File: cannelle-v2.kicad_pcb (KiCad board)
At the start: 2 copper layers, 62 parts, among them P1 USB_OTG, P2 CONN_02X04, P3 CONN_02X22, P4 CONN_02X22, SW1 SW_PUSH, U1 74LS157, U2 ATMEGA16U4-A, U3 SST25VF020B, U4 LD1117S12TR, U5 NCP1117ST33T3G, U6 ICE40HX1K-VQ100, X1 8MHz, X2 IQXO/7X

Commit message: Place components on PCB
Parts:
- moved C14 101.3 mm to (155.8, 40.9)
- moved C21 95.7 mm to (138.8, 52.1), turned to 180 degrees
- moved C20 94.4 mm to (139.8, 50.7), turned to 180 degrees
- moved C30 89.1 mm to (154.2, 53.7)
- moved C23 87.4 mm to (152.4, 51.8), turned to 90 degrees
- moved C24 86.0 mm to (155.4, 55.1)
- moved R11 85.9 mm to (132.5, 51.1), turned to 180 degrees
- moved R10 84.6 mm to (125.5, 63.9), turned to 90 degrees
- moved R12 80.6 mm to (132.5, 53.1), turned to 180 degrees
- moved D3 75.9 mm to (125.5, 60.6), turned to 90 degrees
- moved R9 75.5 mm to (128.7, 63.9), turned to 90 degrees
- moved C18 74.8 mm to (140.0, 68.6), turned to 270 degrees
- moved C17 74.4 mm to (138.4, 67.1), turned to 270 degrees
- moved C22 74.2 mm to (141.2, 49.1), turned to 180 degrees
- moved C25 72.9 mm to (149.4, 49.1), turned to 90 degrees
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
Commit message: Correct wrong label on schem and PCB
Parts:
- moved R7 5.41 mm to (160.1, 79.2), turned to 270 degrees
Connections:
- U1 pad 13: /FPAG_SS -> /FPGA_SS
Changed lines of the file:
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@@
 (kicad_pcb (version 4) (host pcbnew 4.0.2-stable)
   (general
-    (links 254)
-    (no_connects 254)
-    (area 108.667476 35.225999 198.545524 144.534)
+    (links 255)
+    (no_connects 255)
+    (area 0 0 0 0)
     (thickness 1.6)
     (drawings 0)
@@
     (zones 0)
     (modules 62)
-    (nets 134)
+    (nets 133)
   )
   (page A4)
@@
   (net 115 "Net-(U1-Pad11)")
   (net 116 /FLASH_SS)
-  (net 117 /FPAG_SS)
-  (net 118 "Net-(U2-Pad1)")
-  (net 119 "Net-(U2-Pad2)")
-  (net 120 "Net-(U2-Pad12)")
-  (net 121 "Net-(U2-Pad15)")
-  (net 122 "Net-(U2-Pad18)")
-  (net 123 "Net-(U2-Pad19)")
-  (net 124 "Net-(U2-Pad22)")
-  (net 125 "Net-(U2-Pad23)")
-  (net 126 "Net-(U2-Pad25)")
-  (net 127 "Net-(U2-Pad31)")
-  (net 128 "Net-(U2-Pad32)")
-  (net 129 "Net-(U2-Pad33)")
-  (net 130 "Net-(U2-Pad35)")
-  (net 131 /CS_FLASH)
-  (net 132 /FPGA/SYS_CLK)
-  (net 133 "Net-(U6-Pad76)")
+  (net 117 "Net-(U2-Pad1)")
+  (net 118 "Net-(U2-Pad2)")
+  (net 119 "Net-(U2-Pad12)")
+  (net 120 "Net-(U2-Pad15)")
+  (net 121 "Net-(U2-Pad18)")
+  (net 122 "Net-(U2-Pad19)")
+  (net 123 "Net-(U2-Pad22)")
+  (net 124 "Net-(U2-Pad23)")
+  (net 125 "Net-(U2-Pad25)")
+  (net 126 "Net-(U2-Pad31)")
+  (net 127 "Net-(U2-Pad32)")
+  (net 128 "Net-(U2-Pad33)")
+  (net 129 "Net-(U2-Pad35)")
+  (net 130 /CS_FLASH)
+  (net 131 /FPGA/SYS_CLK)
+  (net 132 "Net-(U6-Pad76)")
   (net_class Default "This is the default net class."
     (clearance 0.2)
@@
     (add_net /FLASH_SCK)
     (add_net /FLASH_SS)
-    (add_net /FPAG_SS)
     (add_net /FPGA/DONE)
     (add_net /FPGA/GPIO_3)
@@
   )
   (module Resistors_SMD:R_0402 (layer F.Cu)
-    (at 154.813 78.359)
+    (at 160.147 79.248 270)
     (descr "Resistor SMD 0402, reflow soldering, Vishay (see dcrcw.pdf)")
     (tags "resistor 0402")
     (attr smd)
-    (fp_text reference R7 (at 0 -1.8) (layer F.SilkS)
-      (effects (font (size 1 1) (thickness 0.15)))
-    )
-    (fp_text value 10k (at 0 1.8) (layer F.Fab)
+    (fp_text reference R7 (at 0 -1.8 270) (layer F.SilkS)
+      (effects (font (size 1 1) (thickness 0.15)))
+    )
+    (fp_text value 10k (at 0 1.8 270) (layer F.Fab)
       (effects (font (size 1 1) (thickness 0.15)))
     )
@@
     (fp_line (start 0.25 -0.525) (end -0.25 -0.525) (layer F.SilkS) (width 0.15))
     (fp_line (start -0.25 0.525) (end 0.25 0.525) (layer F.SilkS) (width 0.15))
-    (pad 1 smd rect (at -0.45 0) (size 0.4 0.6) (layers F.Cu F.Paste F.Mask)
-      (net 6 +3V3))
-    (pad 2 smd rect (at 0.45 0) (size 0.4 0.6) (layers F.Cu F.Paste F.Mask)
+    (pad 1 smd rect (at -0.45 0 270) (size 0.4 0.6) (layers F.Cu F.Paste F.Mask)
+      (net 6 +3V3))
+    (pad 2 smd rect (at 0.45 0 270) (size 0.4 0.6) (layers F.Cu F.Paste F.Mask)
       (net 84 /FPGA_SS))
     (model Resistors_SMD.3dshapes/R_0402.wrl
@@
       (net 116 /FLASH_SS))
     (pad 13 smd rect (at -0.635 -5.08) (size 0.635 1.905) (layers F.Cu F.Paste F.Mask)
-      (net 117 /FPAG_SS))
+      (net 84 /FPGA_SS))
     (pad 14 smd rect (at -1.905 -5.08) (size 0.635 1.905) (layers F.Cu F.Paste F.Mask)
       (net 110 /AVR_SS))
@@
     (fp_line (start -5.175 -4.5) (end -6.45 -4.5) (layer F.SilkS) (width 0.15))
     (pad 1 smd rect (at -5.7 -4) (size 1.5 0.55) (layers F.Cu F.Paste F.Mask)
-      (net 118 "Net-(U2-Pad1)"))
+      (net 117 "Net-(U2-Pad1)"))
     (pad 2 smd rect (at -5.7 -3.2) (size 1.5 0.55) (layers F.Cu F.Paste F.Mask)
-      (net 119 "Net-(U2-Pad2)"))
+      (net 118 "Net-(U2-Pad2)"))
     (pad 3 smd rect (at -5.7 -2.4) (size 1.5 0.55) (layers F.Cu F.Paste F.Mask)
       (net 108 "Net-(R3-Pad1)"))
@@
       (net 78 /MISO))
     (pad 12 smd rect (at -4 5.7 90) (size 1.5 0.55) (layers F.Cu F.Paste F.Mask)
-      (net 120 "Net-(U2-Pad12)"))
+      (net 119 "Net-(U2-Pad12)"))
     (pad 13 smd rect (at -3.2 5.7 90) (size 1.5 0.55) (layers F.Cu F.Paste F.Mask)
       (net 24 /RST_AVR))
@@
       (net 6 +3V3))
     (pad 15 smd rect (at -1.6 5.7 90) (size 1.5 0.55) (layers F.Cu F.Paste F.Mask)
-      (net 121 "Net-(U2-Pad15)"))
+      (net 120 "Net-(U2-Pad15)"))
     (pad 16 smd rect (at -0.8 5.7 90) (size 1.5 0.55) (layers F.Cu F.Paste F.Mask)
       (net 4 "Net-(C3-Pad1)"))
@@
       (net 3 "Net-(C2-Pad1)"))
     (pad 18 smd rect (at 0.8 5.7 90) (size 1.5 0.55) (layers F.Cu F.Paste F.Mask)
-      (net 122 "Net-(U2-Pad18)"))
+      (net 121 "Net-(U2-Pad18)"))
     (pad 19 smd rect (at 1.6 5.7 90) (size 1.5 0.55) (layers F.Cu F.Paste F.Mask)
-      (net 123 "Net-(U2-Pad19)"))
+      (net 122 "Net-(U2-Pad19)"))
     (pad 20 smd rect (at 2.4 5.7 90) (size 1.5 0.55) (layers F.Cu F.Paste F.Mask)
       (net 76 /AVR_RX))
@@
       (net 74 /AVR_TX))
     (pad 22 smd rect (at 4 5.7 90) (size 1.5 0.55) (layers F.Cu F.Paste F.Mask)
-      (net 124 "Net-(U2-Pad22)"))
+      (net 123 "Net-(U2-Pad22)"))
     (pad 23 smd rect (at 5.7 4) (size 1.5 0.55) (layers F.Cu F.Paste F.Mask)
-      (net 125 "Net-(U2-Pad23)"))
+      (net 124 "Net-(U2-Pad23)"))
     (pad 24 smd rect (at 5.7 3.2) (size 1.5 0.55) (layers F.Cu F.Paste F.Mask)
       (net 1 /AVCC))
     (pad 25 smd rect (at 5.7 2.4) (size 1.5 0.55) (layers F.Cu F.Paste F.Mask)
-      (net 126 "Net-(U2-Pad25)"))
+      (net 125 "Net-(U2-Pad25)"))
     (pad 26 smd rect (at 5.7 1.6) (size 1.5 0.55) (layers F.Cu F.Paste F.Mask)
       (net 103 /ADC6))
@@
       (net 25 /SPI_SELECT))
     (pad 31 smd rect (at 5.7 -2.4) (size 1.5 0.55) (layers F.Cu F.Paste F.Mask)
-      (net 127 "Net-(U2-Pad31)"))
+      (net 126 "Net-(U2-Pad31)"))
     (pad 32 smd rect (at 5.7 -3.2) (size 1.5 0.55) (layers F.Cu F.Paste F.Mask)
-      (net 128 "Net-(U2-Pad32)"))
+      (net 127 "Net-(U2-Pad32)"))
     (pad 33 smd rect (at 5.7 -4) (size 1.5 0.55) (layers F.Cu F.Paste F.Mask)
-      (net 129 "Net-(U2-Pad33)"))
+      (net 128 "Net-(U2-Pad33)"))
     (pad 34 smd rect (at 4 -5.7 90) (size 1.5 0.55) (layers F.Cu F.Paste F.Mask)
       (net 6 +3V3))
     (pad 35 smd rect (at 3.2 -5.7 90) (size 1.5 0.55) (layers F.Cu F.Paste F.Mask)
-      (net 130 "Net-(U2-Pad35)"))
+      (net 129 "Net-(U2-Pad35)"))
     (pad 36 smd rect (at 2.4 -5.7 90) (size 1.5 0.55) (layers F.Cu F.Paste F.Mask)
       (net 101 /ADC5))
@@
       (net 78 /MISO))
     (pad 1 smd rect (at -1.905 3.175) (size 0.508 1.143) (layers F.Cu F.Paste F.Mask)
-      (net 131 /CS_FLASH))
+      (net 130 /CS_FLASH))
     (model SMD_Packages.3dshapes/SOIC-8-N.wrl
       (at (xyz 0 0 0))
@@
       (net 6 +3V3))
     (pad 15 smd rect (at -7.7 1 225) (size 1.5 0.3) (layers F.Cu F.Paste F.Mask)
-      (net 132 /FPGA/SYS_CLK))
+      (net 131 /FPGA/SYS_CLK))
     (pad 16 smd rect (at -7.7 1.5 225) (size 1.5 0.3) (layers F.Cu F.Paste F.Mask)
       (net 94 "Net-(P4-Pad31)"))
@@
       (net 14 "Net-(D4-Pad1)"))
     (pad 76 smd rect (at 6 -7.7 315) (size 1.5 0.3) (layers F.Cu F.Paste F.Mask)
-      (net 133 "Net-(U6-Pad76)"))
+      (net 132 "Net-(U6-Pad76)"))
     (pad 77 smd rect (at 5.5 -7.7 315) (size 1.5 0.3) (layers F.Cu F.Paste F.Mask)
       (net 8 +1V2))
@@
       (net 2 GND))
     (pad 3 smd rect (at 2.49936 2.10058) (size 1.69926 2.14884) (layers F.Cu F.Paste F.Mask)
-      (net 132 /FPGA/SYS_CLK))
+      (net 131 /FPGA/SYS_CLK))
     (pad 4 smd rect (at 2.49936 -2.10058) (size 1.69926 2.14884) (layers F.Cu F.Paste F.Mask)
       (net 6 +3V3))

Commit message: Ordered labels
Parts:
- ?: renamed from P2; value CONN_02X04 -> (none)
- ?: renamed from P3; value CONN_02X22 -> (none)
- ?: renamed from P4; value CONN_02X22 -> (none)
- C1, C4, C5: value 1u -> (none)
- C10, C11, C12, C13, C14, C15, C16, C17, C18, C19, C20, C21, C22, C23, C24, C25, C26, C27, C28, C29, C30, C6, C7, C8, C9: value 100nF -> (none)
- C2, C3: value 22p -> (none)
- D1, D2, D3, D5: value LED -> (none)
- D4: value D_Schottky -> (none)
- R1: value 370 -> (none)
- R10, R12, R9: value 2.2k -> (none)
- R11, R4, R5, R7, R8: value 10k -> (none)
- R13, R2, R3: value 22 -> (none)
- R6: value 120 -> (none)
- SW1: value SW_PUSH -> (none)
- U1: value 74LS157 -> (none)
- U2: value ATMEGA16U4-A -> (none)
- U3: value SST25VF020B -> (none)
- U4: value LD1117S12TR -> (none)
- U5: value NCP1117ST33T3G -> (none)
- U6: value ICE40HX1K-VQ100 -> ICE40HX1K
- X1: value 8MHz -> (none)
- X2: value IQXO/7X -> (none)
- moved SW1 31.8 mm to (147.3, 101.1)
- moved C11 8.72 mm to (162.9, 84.5)
- moved C14 8.58 mm to (159.5, 48.6), turned to 45 degrees
- moved U3 8.54 mm to (161.4, 79.1)
- moved U1 8.03 mm to (159.6, 95.0)
- moved R5 7.80 mm to (156.2, 87.0)
- moved R8 7.80 mm to (157.7, 87.0)
- moved R7 7.78 mm to (159.4, 87.0)
- moved ? 7.56 mm to (169.2, 98.0)
- moved ? 6.56 mm to (118.0, 98.0)
- moved ? 5.79 mm to (150.1, 84.7)
- moved P1 3.94 mm to (132.2, 117.0)
- moved R2 3.01 mm to (131.4, 110.2)
- moved R3 3.01 mm to (133.0, 110.2)
- moved C17 2.87 mm to (136.4, 65.0), turned to 225 degrees
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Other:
- board text added: "Cannelle Project (c) Ronan Gailard 2016"
- board text added: "Made with love in Boston, US"

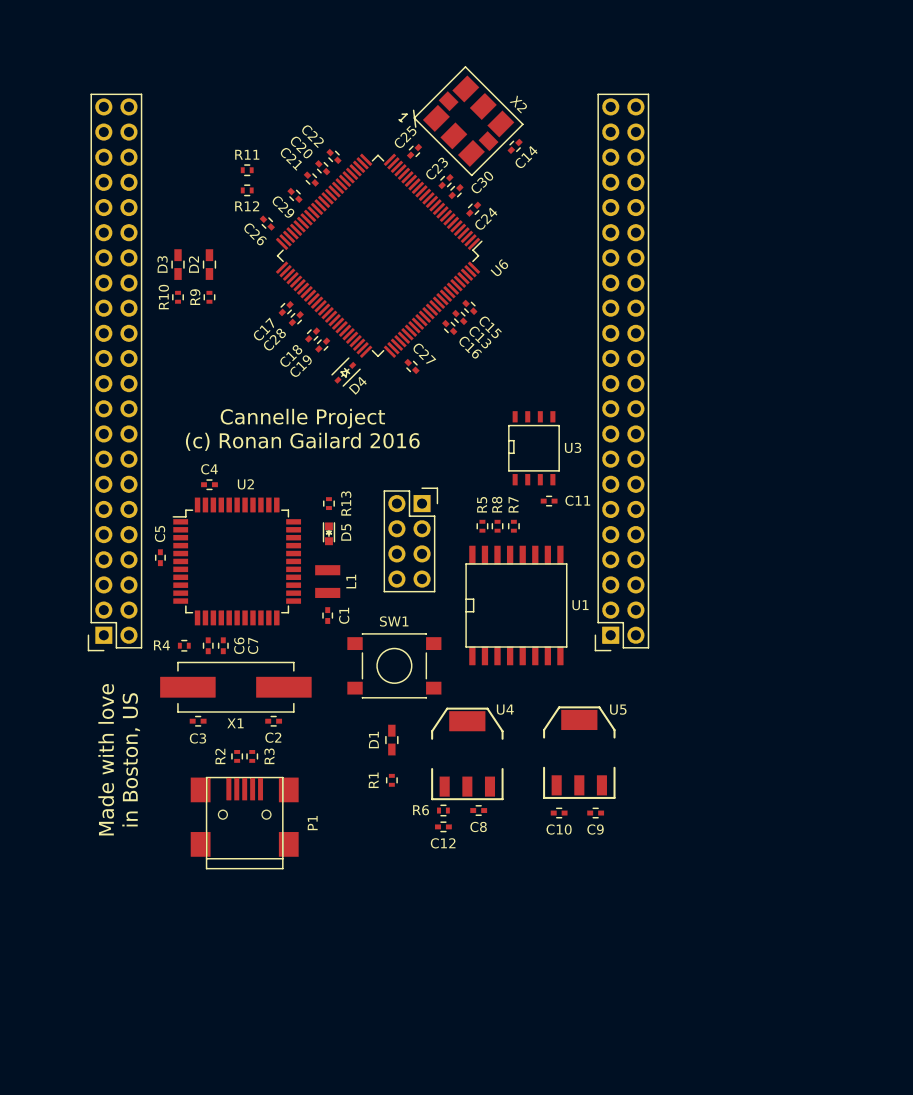
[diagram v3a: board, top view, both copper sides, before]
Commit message: Design first connections on PCB
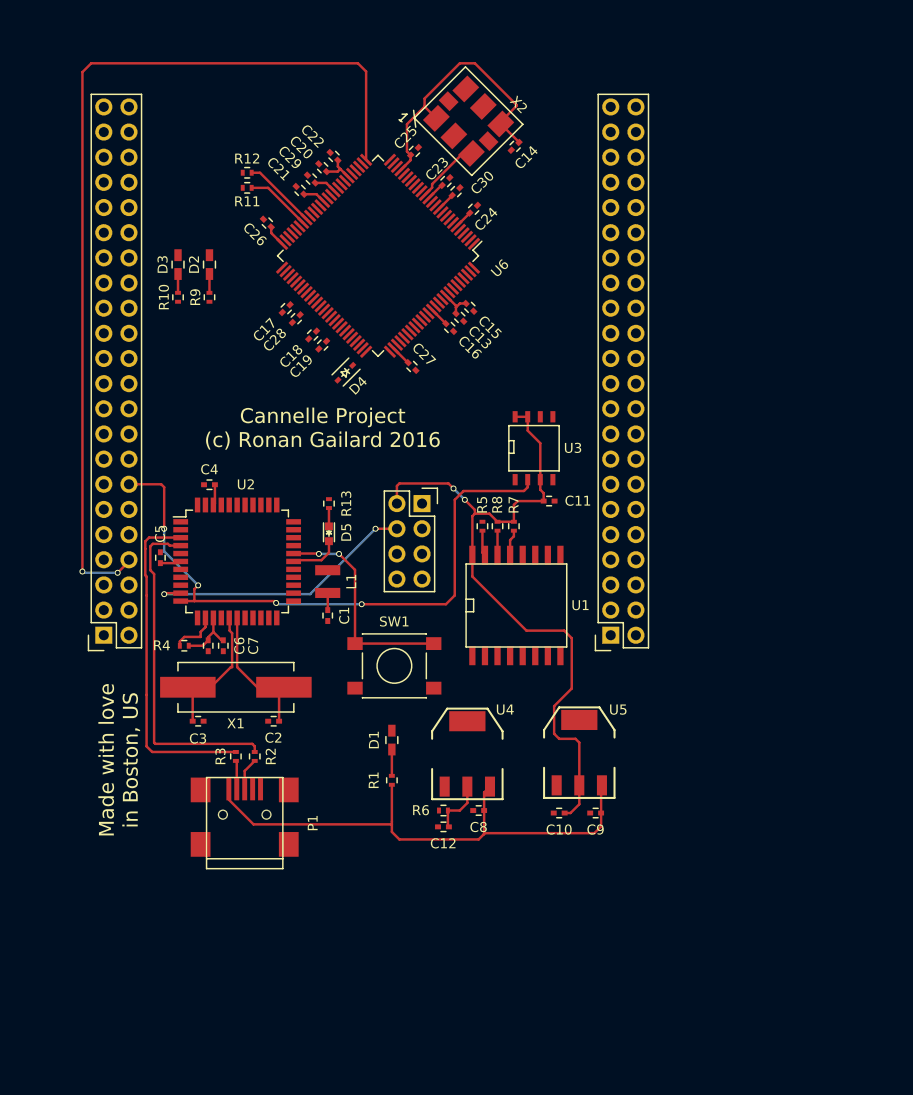
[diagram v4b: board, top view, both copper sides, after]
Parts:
- L1: value 10uH -> (none)
- moved C29 2.33 mm to (138.9, 51.9)
- moved R2 1.78 mm to (133.2, 110.2), turned to 270 degrees
- moved R11 1.78 mm to (132.5, 52.8)
- moved R12 1.78 mm to (132.5, 51.3)
- moved R3 1.65 mm to (131.3, 110.2), turned to 270 degrees
- moved C21 1.62 mm to (137.8, 53.1)
- turned D2 to 90 degrees
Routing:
- net +3V3: track 0.00 -> 124.8 mm, vias 0 -> 2
- net Net-(P4-Pad8): track 0.00 -> 94.1 mm, vias 0 -> 2
- net /MISO: track 0.00 -> 63.2 mm, vias 0 -> 4
- net +5V: track 0.00 -> 54.5 mm
- net Net-(R2-Pad1): track 0.00 -> 34.1 mm
- net Net-(R3-Pad1): track 0.00 -> 33.7 mm
- net /FPGA/ICE40_RESET: track 0.00 -> 28.9 mm, vias 0 -> 2
- net /AVR_MOSI: track 0.00 -> 27.9 mm, vias 0 -> 2
- net Net-(C2-Pad1): track 0.00 -> 14.2 mm
- net Net-(C3-Pad1): track 0.00 -> 14.0 mm
- net /FPGA/DONE: track 0.00 -> 12.6 mm
- net +1V2: track 0.00 -> 11.9 mm
- net /FPGA/SYS_CLK: track 0.00 -> 6.63 mm
- net /RST_AVR: track 0.00 -> 4.85 mm
- net Net-(P1-Pad3): track 0.00 -> 3.25 mm
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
